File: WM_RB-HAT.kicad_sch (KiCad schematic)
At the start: 85 parts, among them J1 AudioJack3, J2 AudioJack3, J3 2x20 Pins, J4 AudioJack3, J5 AudioJack3, J6 Audio In, J7 Audio Out, Q1 BC817, Q2 BFS17A, U1 WM8960, U3 74AHC1G14, U4 MCP1711T-33 /OT, X1 XO32, Y1 24MHz

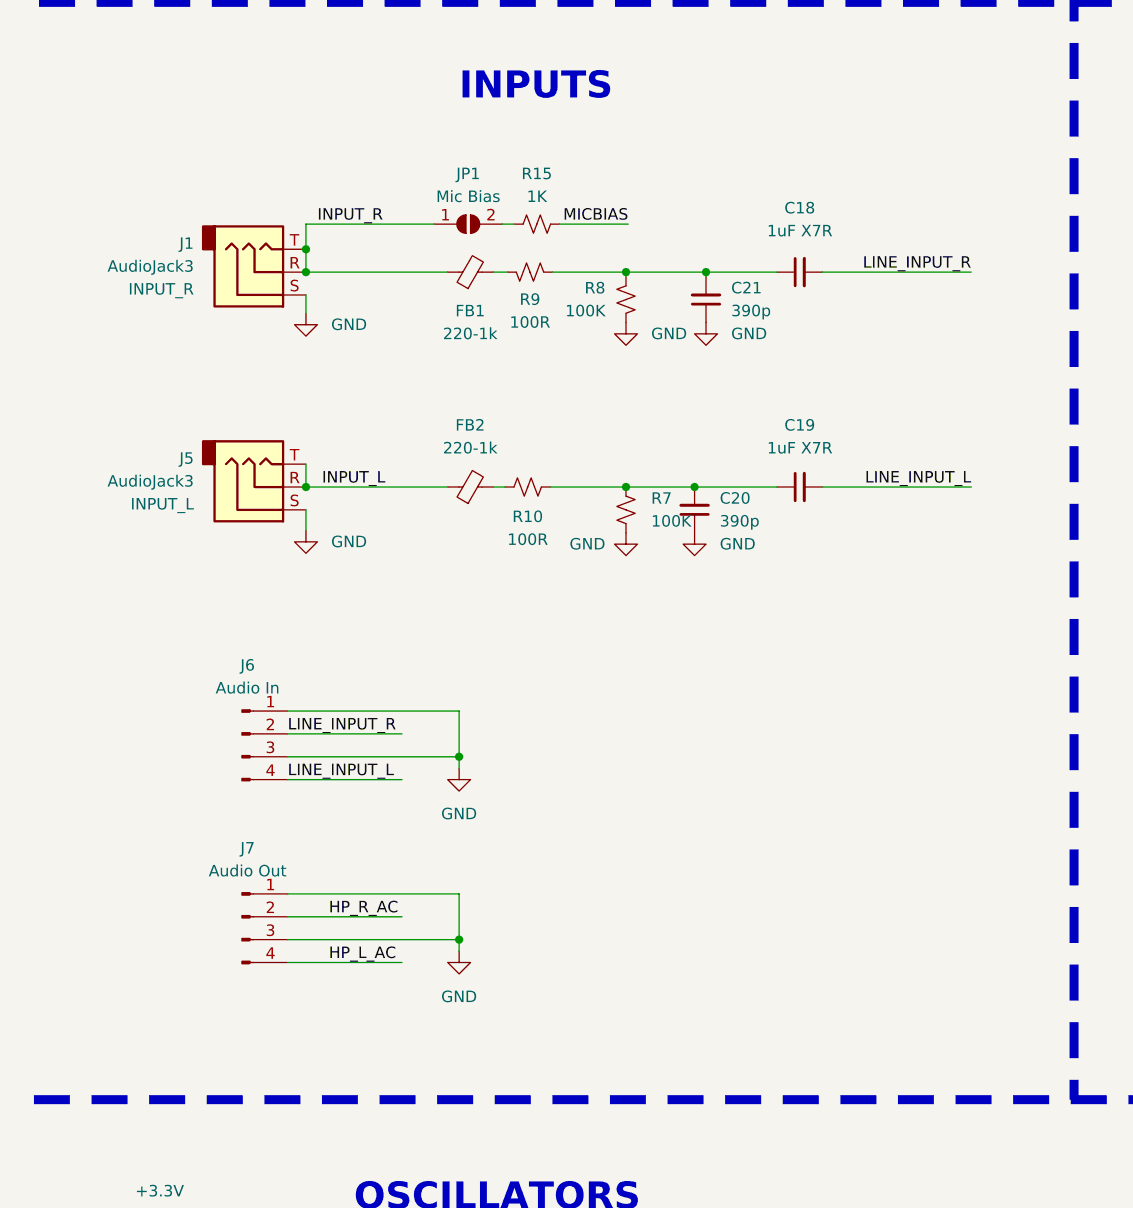
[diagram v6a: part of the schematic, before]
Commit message: Add SSSS213202 slide switch library, PCB and schematic updates
- Add Alps SSSS213202 SPDT switch: symbol, footprint, 3D model (LCSC C115375)
- Register switch libraries in sym-lib-table and fp-lib-table
- Schematic and PCB layout updates
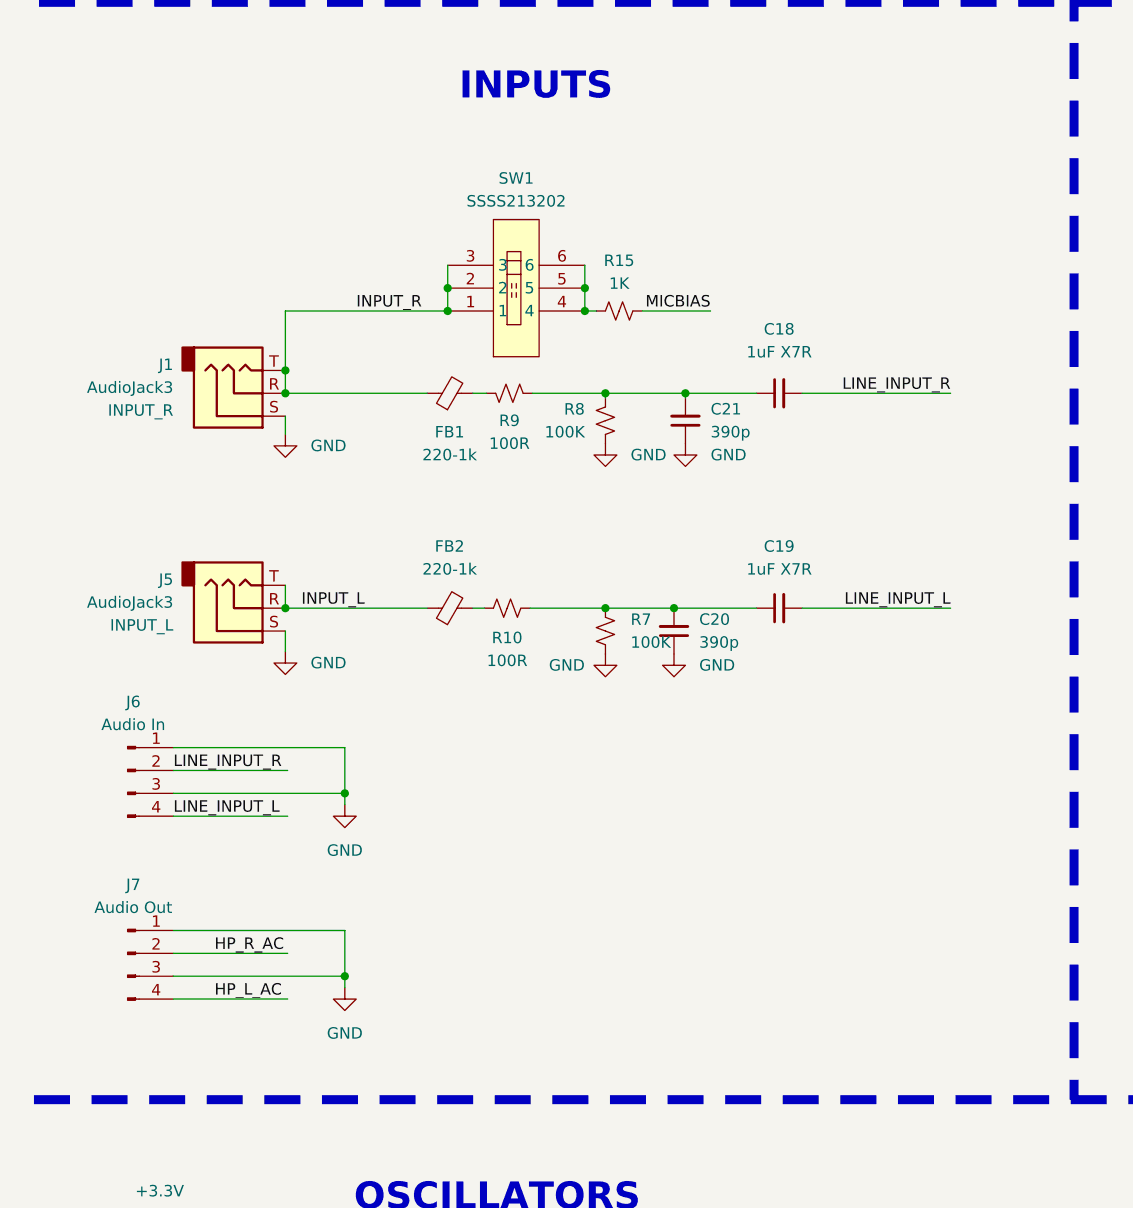
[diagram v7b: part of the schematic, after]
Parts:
- removed JP1: Mic Bias, ArduinoModules:SolderJumper-2_P1.3mm_Open_TrianglePad1.0x1.5mm, symbol 0Arduino_Modules:SolderJumper_2_Open
- added SW1: SSSS213202, SSSS213202:SW-TH_SSSS213202, symbol SSSS213202:SSSS213202
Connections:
- net INPUT_R: now also SW1.1, SW1.2, SW1.3
- net at R15.1: now also SW1.4, SW1.5, SW1.6
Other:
- moved on the sheet: C18, C19, C20, C21, FB1, FB2, J1, J5, J6, J7, R10, R15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

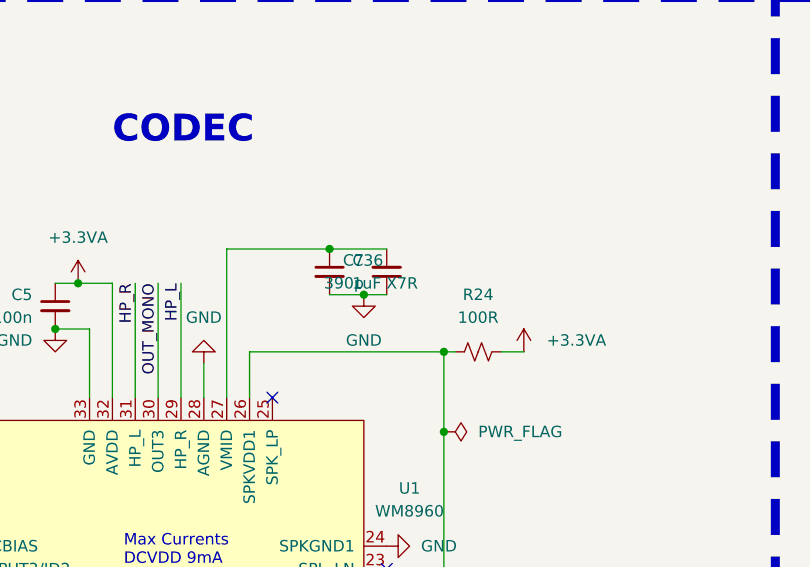
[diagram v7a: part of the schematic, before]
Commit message: PCB routing progress, fix C36 VMID cap to 4.7uF X7R
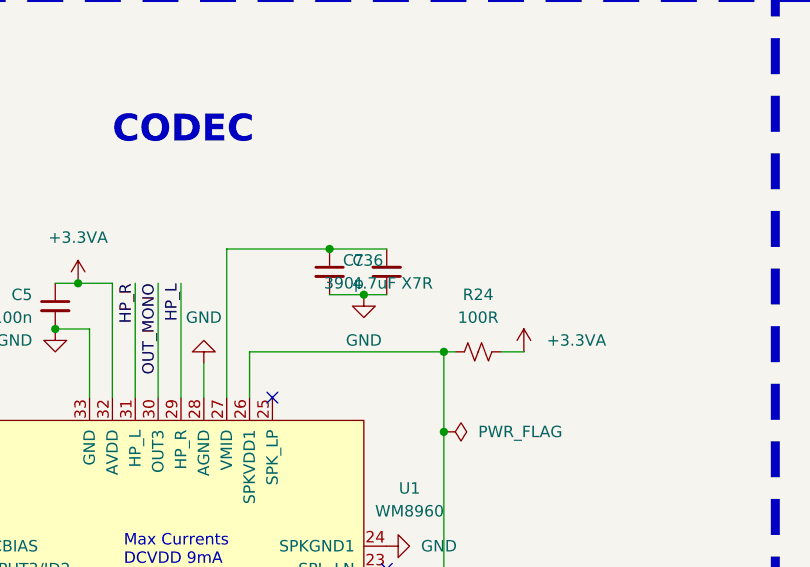
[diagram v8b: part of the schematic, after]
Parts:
- C36: value 1uF X7R -> 4.7uF X7R; LCSC C28323 -> C87998
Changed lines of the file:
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@@
 			)
 		)
-		(property "Value" "1uF X7R"
+		(property "Value" "4.7uF X7R"
 			(at 228.6 128.2762 0)
 			(effects
@@
 			)
 		)
-		(property "LCSC" "C28323"
+		(property "LCSC" "C87998"
 			(at 226.06 127 0)
 			(effects
